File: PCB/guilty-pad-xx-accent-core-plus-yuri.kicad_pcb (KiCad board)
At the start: 2 copper layers, 347.8 x 124 mm, 287 parts, among them J1 Conn_01x04_Socket, J2 Conn_01x04_MountingPin, SW1 SW_Push, SW10 SW_Push, SW11 SW_Push, SW12 SW_Push, SW13 SW_Push, SW14 SW_Push, SW15 SW_Push, SW16 SW_Push, SW17 SW_Push, SW18 SW_Push, SW19 SW_Push, SW2 SW_Push, SW20 SW_Push, SW21 SW_Push, SW22 SW_Push, SW23 SW_Push, SW24 SW_Push, SW25 SW_Push, SW26 SW_Push, SW27 SW_Push, SW28 SW_Push, SW29 SW_Push, SW3 SW_Push, SW30 SW_Push, SW31 SW_Push, SW32 SW_Push, SW33 SW_Push, SW34 SW_Push, SW35 SW_Push, SW36 SW_Push, SW37 SW_Push, SW38 SW_Push, SW39 SW_Push, SW4 SW_Push, SW40 SW_Push, SW41 SW_Push, SW42 SW_Push, SW43 SW_Push, SW44 SW_Push, SW45 SW_Push, SW46 SW_Push, SW47 SW_Push, SW48 SW_Push, SW49 SW_Push, SW5 SW_Push, SW50 SW_Push, SW51 SW_Push, SW52 SW_Push, SW53 SW_Push, SW54 SW_Push, SW55 SW_Push, SW56 SW_Push, SW57 SW_Push, SW58 SW_Push, SW59 SW_Push, SW6 SW_Push, SW60 SW_Push, SW61 SW_Push, SW62 SW_Push, SW63 SW_Push, SW64 SW_Push, SW65 SW_Push, SW66 SW_Push, SW67 SW_Push, SW68 SW_Push, SW69 SW_Push, SW7 SW_Push, SW70 SW_Push, SW71 SW_Push, SW72 SW_Push, SW73 SW_Push, SW74 SW_Push, SW75 SW_Push, SW76 SW_Push, SW77 SW_Push, SW78 SW_Push, SW79 SW_Push, SW8 SW_Push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

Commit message: update with fixed xrd footprint, fix oled pinout, fix some silkscreen stuff, idk what else
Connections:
- J1 pad 1: +3V3 -> GND
- J1 pad 2: GND -> +3V3
- J1 pad 3: /I2C_SDA -> /I2C_SCL
- J1 pad 4: /I2C_SCL -> /I2C_SDA
- U1 pad 35: /I2C_SDA -> /I2C_SCL
- U1 pad 36: /I2C_SCL -> /I2C_SDA
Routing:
- net GND: track 2426.8 -> 2428.5 mm
- net +3V3: track 376.3 -> 377.8 mm
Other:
- board text added: "+"
- board text added: "-"

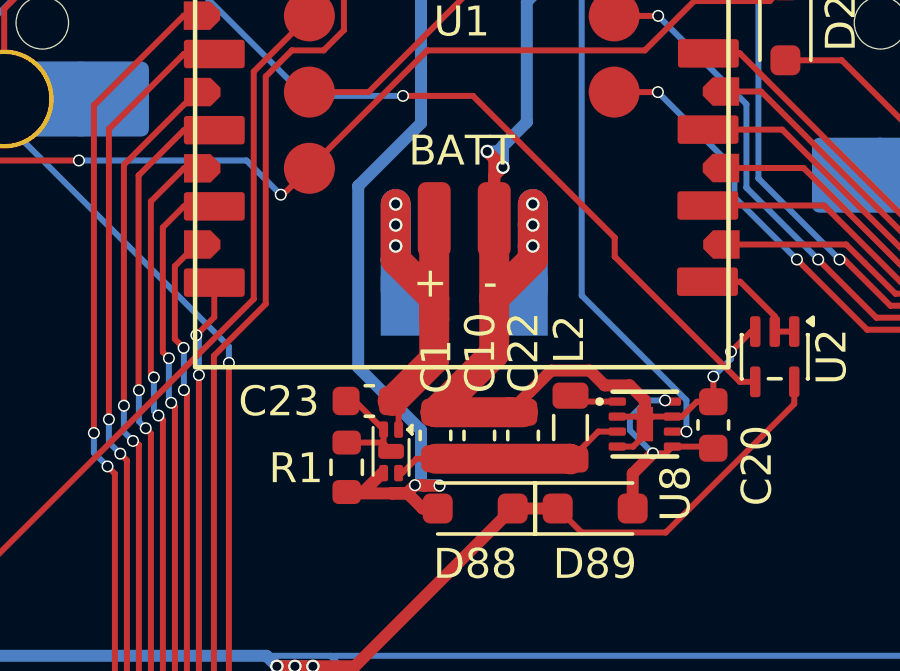
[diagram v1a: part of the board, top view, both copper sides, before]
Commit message: update silkscreening
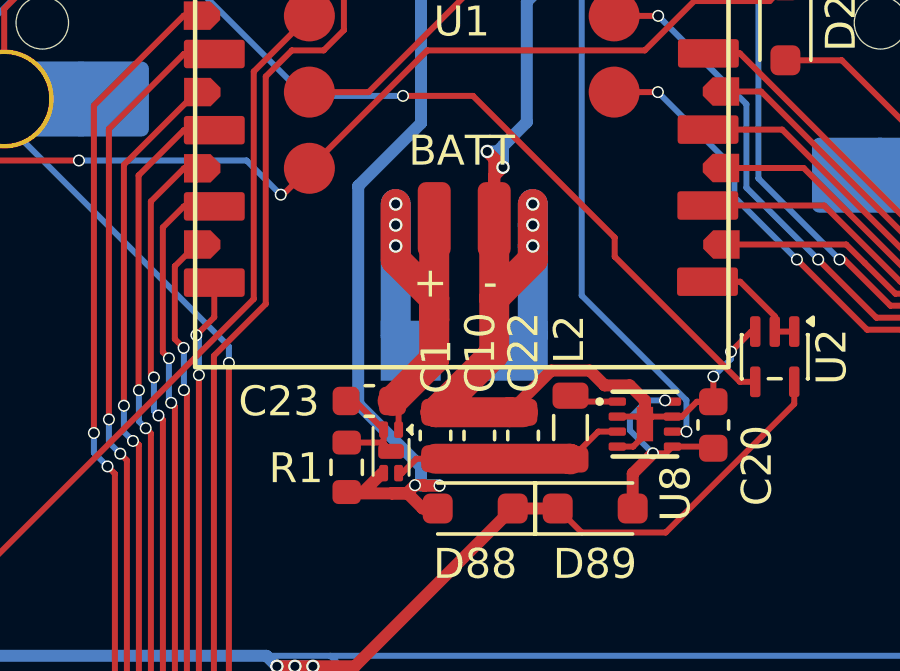
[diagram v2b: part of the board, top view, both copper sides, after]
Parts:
- moved TP1 1.50 mm to (55.5, 49.0)
- moved TP2 1.50 mm to (59.0, 49.0)
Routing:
- net GND: track 2428.5 -> 2430.7 mm
- net /VBAT: track 14.7 -> 16.9 mm

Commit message: round corners
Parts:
- removed the G*** at (184.1, 139.8)

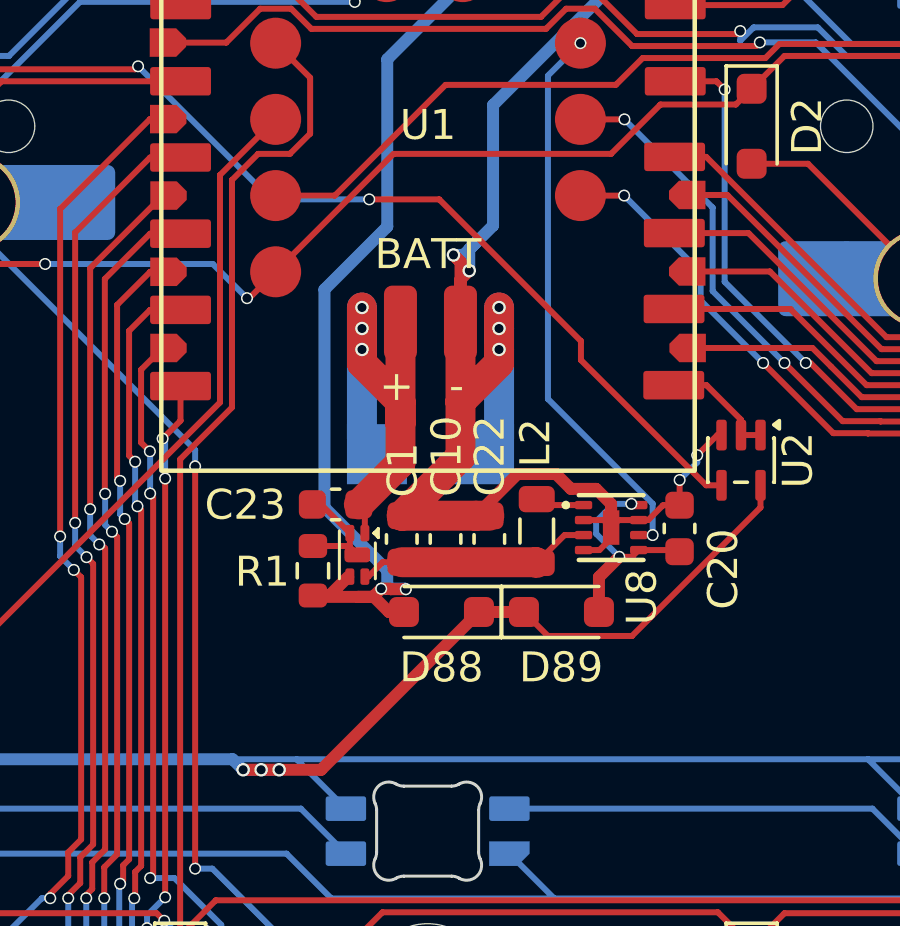
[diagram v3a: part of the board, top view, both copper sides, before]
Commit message: fix missing gnd for sip32408
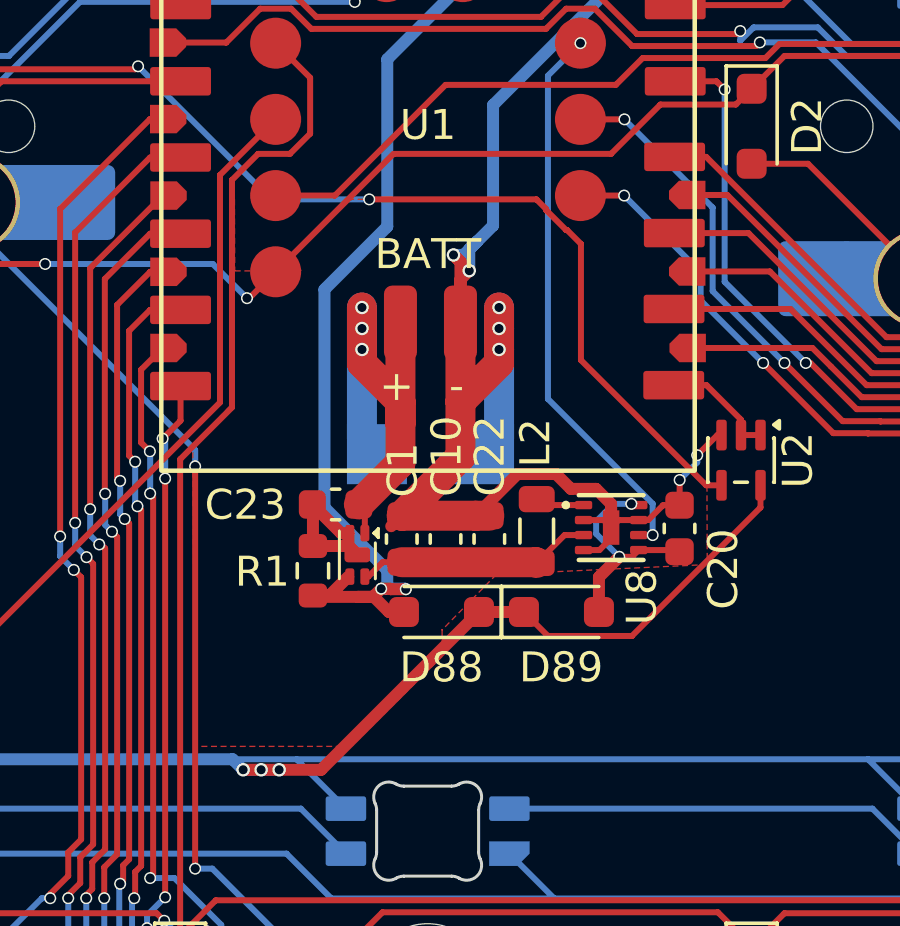
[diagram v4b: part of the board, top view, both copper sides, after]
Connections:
- C23 pad 1: Net-(U3-EP) -> GND
- R1 pad 1: Net-(U3-EP) -> GND
- U3 pad 2: Net-(U3-EP) -> GND
- U3 pad 5: Net-(U3-EP) -> GND
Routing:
- net GND: track 2430.7 -> 2436.7 mm
- net Net-(U3-EP): track 3.78 -> 0.00 mm
- net /LED_CONTROL: track 39.2 -> 41.1 mm
- added copper zone on F.Cu, net GND
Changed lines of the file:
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@@
 			(layers "F.Cu" "F.Mask" "F.Paste")
 			(roundrect_rratio 0.25)
-			(net "Net-(U3-EP)")
+			(net "GND")
 			(pinfunction "GND_2")
 			(pintype "power_out")
@@
 			(layers "F.Cu" "F.Mask" "F.Paste")
 			(roundrect_rratio 0.25)
-			(net "Net-(U3-EP)")
+			(net "GND")
 			(pinfunction "EP_5")
 			(pintype "passive")
@@
 			(layers "F.Cu" "F.Mask" "F.Paste")
 			(roundrect_rratio 0.25)
-			(net "Net-(U3-EP)")
+			(net "GND")
 			(pintype "passive")
 		)
@@
 			(layers "F.Cu" "F.Mask" "F.Paste")
 			(roundrect_rratio 0.25)
-			(net "Net-(U3-EP)")
+			(net "GND")
 			(pintype "passive")
 		)
@@
 	)
 	(segment
+		(start 54.80625 52.38625)
+		(end 54.50625 52.08625)
+		(width 0.4)
+		(layer "F.Cu")
+		(net "GND")
+	)
+	(segment
 		(start 35.47 56.33)
 		(end 32.0575 56.33)
@@
 	)
 	(segment
+		(start 54.26125 51.66125)
+		(end 54.50625 51.66125)
+		(width 0.4)
+		(layer "F.Cu")
+		(net "GND")
+	)
+	(segment
 		(start 375.575 138.0125)
 		(end 373.5475 140.04)
@@
 	)
 	(segment
+		(start 53.32625 52.09125)
+		(end 54.51125 52.09125)
+		(width 0.4)
+		(layer "F.Cu")
+		(net "GND")
+	)
+	(segment
 		(start 51.133231 31.170337)
 		(end 54.683601 31.170337)
@@
 	)
 	(segment
+		(start 54.50625 52.08625)
+		(end 54.50625 51.66125)
+		(width 0.4)
+		(layer "F.Cu")
+		(net "GND")
+	)
+	(segment
 		(start 64.99645 50.73125)
 		(end 65.54625 50.73125)
@@
 	)
 	(segment
+		(start 53.32625 50.72625)
+		(end 53.30625 50.70625)
+		(width 0.4)
+		(layer "F.Cu")
+		(net "GND")
+	)
+	(segment
 		(start 62.76287 50.18625)
 		(end 61.924856 50.18625)
@@
 	)
 	(segment
+		(start 53.32625 52.09125)
+		(end 53.32625 50.72625)
+		(width 0.4)
+		(layer "F.Cu")
+		(net "GND")
+	)
+	(segment
+		(start 56.28625 51.08125)
+		(end 55.93625 51.43125)
+		(width 0.4)
+		(layer "F.Cu")
+		(net "GND")
+	)
+	(segment
 		(start 63.26625 50.85)
 		(end 63.26625 50.68963)
@@
 	)
 	(segment
+		(start 54.51125 52.09125)
+		(end 54.80625 52.38625)
+		(width 0.4)
+		(layer "F.Cu")
+		(net "GND")
+	)
+	(segment
 		(start 355.5475 140.04)
 		(end 354.4975 140.04)
@@
 	)
 	(segment
+		(start 53.30625 50.70625)
+		(end 54.26125 51.66125)
+		(width 0.4)
+		(layer "F.Cu")
+		(net "GND")
+	)
+	(segment
 		(start 61.924856 50.18625)
 		(end 61.429856 49.69125)
@@
 	)
 	(segment
-		(start 66.4325 50.0675)
-		(end 62.26 45.895)
+		(start 61.093 40.853)
+		(end 60.776393 40.536393)
 		(width 0.2)
 		(layer "F.Cu")
@@
 	)
 	(segment
-		(start 66.945 50.0675)
-		(end 66.4325 50.0675)
+		(start 35.72 34.8)
+		(end 36.6761 35.7561)
 		(width 0.2)
 		(layer "F.Cu")
@@
 	(segment
 		(start 62.26 45.895)
-		(end 62.26 45.26)
+		(end 62.26 42.02)
 		(width 0.2)
 		(layer "F.Cu")
@@
 	)
 	(segment
-		(start 35.72 34.8)
-		(end 36.6761 35.7561)
+		(start 61.8 41.56)
+		(end 61.766654 41.56)
 		(width 0.2)
 		(layer "F.Cu")
@@
 	)
 	(segment
-		(start 57.536393 40.536393)
-		(end 55.203714 40.536393)
+		(start 39.514775 36.2)
+		(end 47.398251 36.2)
 		(width 0.2)
 		(layer "F.Cu")
@@
 	)
 	(segment
-		(start 39.514775 36.2)
-		(end 47.398251 36.2)
+		(start 66.4325 50.0675)
+		(end 62.26 45.895)
+		(width 0.2)
+		(layer "F.Cu")
+		(net "/LED_CONTROL")
+	)
+	(segment
+		(start 66.945 50.0675)
+		(end 66.4325 50.0675)
+		(width 0.2)
+		(layer "F.Cu")
+		(net "/LED_CONTROL")
+	)
+	(segment
+		(start 60.776393 40.536393)
+		(end 55.203714 40.536393)
 		(width 0.2)
 		(layer "F.Cu")
@@
 	)
 	(segment
+		(start 61.093 40.886346)
+		(end 61.093 40.853)
+		(width 0.2)
+		(layer "F.Cu")
+		(net "/LED_CONTROL")
+	)
+	(segment
+		(start 61.766654 41.56)
+		(end 61.093 40.886346)
+		(width 0.2)
+		(layer "F.Cu")
+		(net "/LED_CONTROL")
+	)
+	(segment
 		(start 36.6761 35.7561)
 		(end 39.070875 35.7561)
@@
 	)
 	(segment
-		(start 62.26 45.26)
-		(end 57.536393 40.536393)
+		(start 62.26 42.02)
+		(end 61.8 41.56)
 		(width 0.2)
 		(layer "F.Cu")
@@
 	)
 	(segment
-		(start 53.32625 52.09125)
-		(end 54.51125 52.09125)
-		(width 0.2)
-		(layer "F.Cu")
-		(net "Net-(U3-EP)")
-	)
-	(segment
-		(start 54.55625 52.13625)
-		(end 54.55625 51.66125)
-		(width 0.2)
-		(layer "F.Cu")
-		(net "Net-(U3-EP)")
-	)
-	(segment
-		(start 54.51125 52.09125)
-		(end 54.80625 52.38625)
-		(width 0.2)
-		(layer "F.Cu")
-		(net "Net-(U3-EP)")
-	)
-	(segment
-		(start 54.80625 52.38625)
-		(end 54.55625 52.13625)
-		(width 0.2)
-		(layer "F.Cu")
-		(net "Net-(U3-EP)")
-	)
-	(segment
-		(start 53.60125 50.70625)
-		(end 54.55625 51.66125)
-		(width 0.2)
-		(layer "F.Cu")
-		(net "Net-(U3-EP)")
-	)
-	(segment
 		(start 88.88 67.925)
 		(end 87 67.925)
@@
 		(net "Net-(LED10-DOUT)")
 	)
+	(zone
+		(net "GND")
+		(layer "F.Cu")
+		(hatch edge 0.5)
+		(connect_pads
+			(clearance 0.5)
+		)
+		(min_thickness 0.25)
+		(fill yes
+			(thermal_gap 0.5)
+			(thermal_bridge_width 0.5)
+			(island_removal_mode 0)
+		)
+		(polygon
+			(pts
+				(xy 57.6325 54.88) (xy 57.6325 55.77) (xy 54.607753 58.77) (xy 49.38398 58.77) (xy 49.32 48.78)
+				(xy 50.59 47.39) (xy 50.628 43.996429) (xy 50.628 39.890686) (xy 50.71 40.536393) (xy 50.72 42.92)
+				(xy 52.93 42.92) (xy 52.7 42.41) (xy 54.496607 40.536393) (xy 60.767636 40.536393) (xy 62.26 42.011151)
+				(xy 62.26 45.83) (xy 66.46 50.08) (xy 66.47 52.71) (xy 59.44 53.04) (xy 57.63 54.89) (xy 57.63 54.88)
+				(xy 57.64 54.89) (xy 57.63 54.88) (xy 57.64 54.87) (xy 57.63 54.88)
+			)
+		)
+	)
 	(embedded_fonts no)
